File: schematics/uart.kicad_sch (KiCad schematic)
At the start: 7 parts, among them J10 myBus, J9 Pins, U8 74HC238, U9 W65C51N, X1 CXO_DIP8

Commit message: Fix errors in schematics
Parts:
- renumbered J9 to J7, J10 to J8

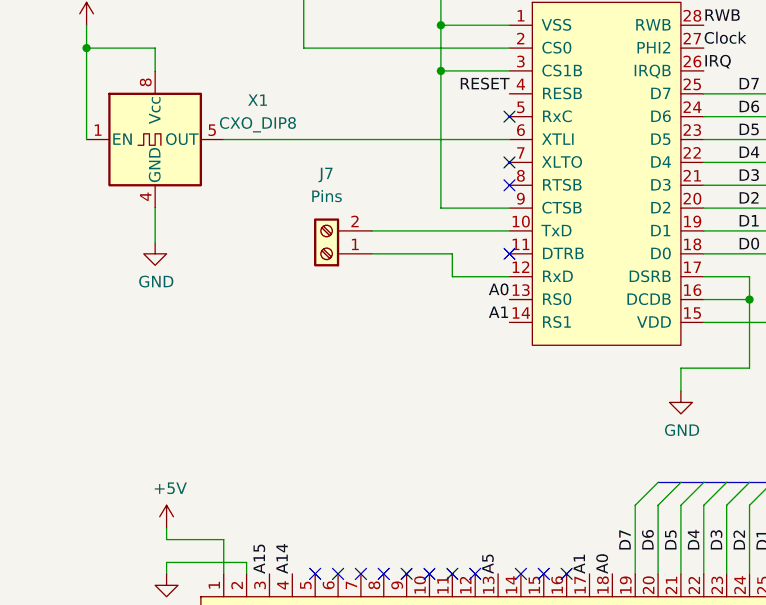
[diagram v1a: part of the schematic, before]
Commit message: Update shematics for UART & ESP
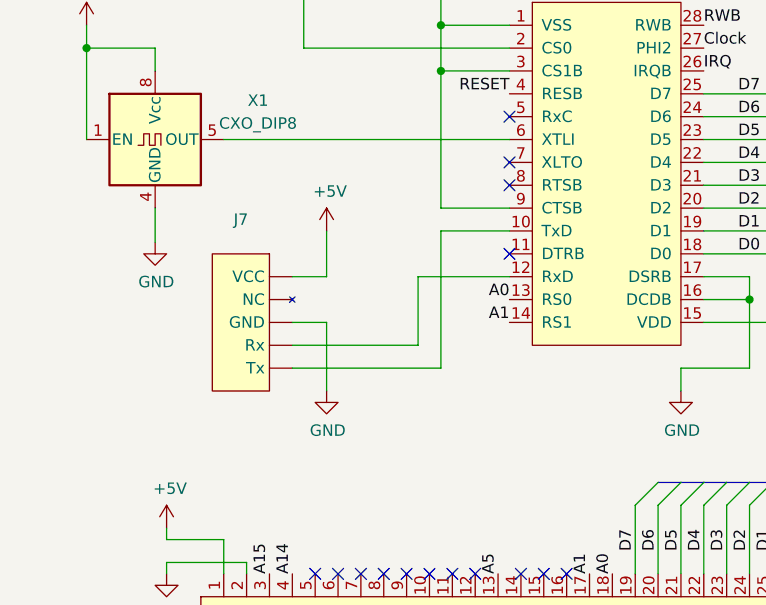
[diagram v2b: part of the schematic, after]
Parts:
- removed J7: Pins, symbol Connector:Screw_Terminal_01x02
- added J7: ~, symbol 6502:UART_connector
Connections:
- net +5V: now also J7. (VCC)
- net GND: now also J7. (VCC)
- net at U9.10 (TxD): now also J7. (VCC)
- net at U9.12 (RxD): now also J7. (VCC)
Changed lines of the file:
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@@
-		)
-	)
-	(wire
-		(pts
-			(xy 105.41 100.33) (xy 120.65 100.33)
-		)
-		(stroke
-			(width 0)
-			(type default)
 		)
 	)
@@
 		)
 	)
+	(wire
+		(pts
+			(xy 100.33 110.49) (xy 100.33 118.11)
+		)
+		(stroke
+			(width 0)
+			(type default)
+		)
+	)
 	(bus
 		(pts
@@
 	(wire
 		(pts
-			(xy 114.3 105.41) (xy 120.65 105.41)
+			(xy 113.03 100.33) (xy 120.65 100.33)
 		)
 		(stroke
@@
 	(wire
 		(pts
+			(xy 96.52 110.49) (xy 100.33 110.49)
+		)
+		(stroke
+			(width 0)
+			(type default)
+		)
+	)
+	(wire
+		(pts
 			(xy 88.9 90.17) (xy 120.65 90.17)
 		)
@@
 		)
 	)
+	(wire
+		(pts
+			(xy 110.49 105.41) (xy 110.49 113.03)
+		)
+		(stroke
+			(width 0)
+			(type default)
+		)
+	)
 	(bus
 		(pts
@@
 		)
 	)
+	(wire
+		(pts
+			(xy 96.52 105.41) (xy 100.33 105.41)
+		)
+		(stroke
+			(width 0)
+			(type default)
+		)
+	)
+	(wire
+		(pts
+			(xy 120.65 105.41) (xy 110.49 105.41)
+		)
+		(stroke
+			(width 0)
+			(type default)
+		)
+	)
 	(bus
 		(pts
@@
 	(wire
 		(pts
+			(xy 113.03 115.57) (xy 113.03 100.33)
+		)
+		(stroke
+			(width 0)
+			(type default)
+		)
+	)
+	(wire
+		(pts
 			(xy 68.58 67.31) (xy 68.58 68.58)
 		)
@@
 	(wire
 		(pts
-			(xy 105.41 102.87) (xy 114.3 102.87)
-		)
-		(stroke
-			(width 0)
-			(type default)
-		)
-	)
-	(wire
-		(pts
 			(xy 107.95 64.77) (xy 111.76 64.77)
 		)
@@
 	(wire
 		(pts
+			(xy 110.49 113.03) (xy 96.52 113.03)
+		)
+		(stroke
+			(width 0)
+			(type default)
+		)
+	)
+	(wire
+		(pts
 			(xy 119.38 64.77) (xy 123.19 64.77)
 		)
@@
 	(wire
 		(pts
+			(xy 100.33 105.41) (xy 100.33 100.33)
+		)
+		(stroke
+			(width 0)
+			(type default)
+		)
+	)
+	(wire
+		(pts
 			(xy 149.86 130.81) (xy 149.86 138.43)
 		)
@@
 	(wire
 		(pts
-			(xy 114.3 102.87) (xy 114.3 105.41)
+			(xy 96.52 115.57) (xy 113.03 115.57)
 		)
 		(stroke
@@
 	)
 	(symbol
-		(lib_id "Connector:Screw_Terminal_01x02")
-		(at 100.33 102.87 180)
+		(lib_id "6502:UART_connector")
+		(at 91.44 114.3 270)
 		(unit 1)
 		(exclude_from_sim no)
@@
 		(fields_autoplaced yes)
 		(property "Reference" "J7"
-			(at 100.33 93.98 0)
-			(effects
-				(font
-					(size 1.27 1.27)
-				)
-			)
-		)
-		(property "Value" "Pins"
-			(at 100.33 96.52 0)
+			(at 90.805 99.06 90)
+			(effects
+				(font
+					(size 1.27 1.27)
+				)
+			)
+		)
+		(property "Value" "~"
+			(at 90.805 101.6 90)
 			(effects
 				(font
@@
 		)
 		(property "Footprint" ""
-			(at 100.33 102.87 0)
-			(effects
-				(font
-					(size 1.27 1.27)
-				)
-				(hide yes)
-			)
-		)
-		(property "Datasheet" "~"
-			(at 100.33 102.87 0)
-			(effects
-				(font
-					(size 1.27 1.27)
-				)
-				(hide yes)
-			)
-		)
-		(property "Description" "Generic screw terminal, single row, 01x02, script generated (kicad-library-utils/schlib/autogen/connector/)"
-			(at 100.33 102.87 0)
+			(at 91.44 114.3 0)
+			(effects
+				(font
+					(size 1.27 1.27)
+				)
+				(hide yes)
+			)
+		)
+		(property "Datasheet" ""
+			(at 91.44 114.3 0)
+			(effects
+				(font
+					(size 1.27 1.27)
+				)
+				(hide yes)
+			)
+		)
+		(property "Description" ""
+			(at 91.44 114.3 0)
+			(effects
+				(font
+					(size 1.27 1.27)
+				)
+				(hide yes)
+			)
+		)
+		(pin ""
+		)
+		(pin ""
+		)
+		(pin ""
+		)
+		(pin ""
+		)
+		(pin ""
+		)
+		(instances
+			(project ""
+				(path "/03a78ca6-eaff-4f05-be7b-36cd15f8b56d/e1937880-b4d5-4732-8378-398cc9358f14"
+					(reference "J7")
+					(unit 1)
+				)
+			)
+		)
+	)
+	(symbol
+		(lib_id "power:GND")
+		(at 100.33 118.11 0)
+		(unit 1)
+		(exclude_from_sim no)
+		(in_bom yes)
+		(on_board yes)
+		(dnp no)
+		(property "Reference" "#PWR0101"
+			(at 100.33 124.46 0)
+			(effects
+				(font
+					(size 1.27 1.27)
+				)
+				(hide yes)
+			)
+		)
+		(property "Value" "GND"
+			(at 100.457 122.5042 0)
+			(effects
+				(font
+					(size 1.27 1.27)
+				)
+			)
+		)
+		(property "Footprint" ""
+			(at 100.33 118.11 0)
+			(effects
+				(font
+					(size 1.27 1.27)
+				)
+				(hide yes)
+			)
+		)
+		(property "Datasheet" ""
+			(at 100.33 118.11 0)
+			(effects
+				(font
+					(size 1.27 1.27)
+				)
+				(hide yes)
+			)
+		)
+		(property "Description" "Power symbol creates a global label with name \"GND\" , ground"
+			(at 100.33 118.11 0)
 			(effects
 				(font
@@
 		)
 		(pin "1"
-		)
-		(pin "2"
 		)
 		(instances
 			(project "markus"
 				(path "/03a78ca6-eaff-4f05-be7b-36cd15f8b56d/e1937880-b4d5-4732-8378-398cc9358f14"
-					(reference "J7")
+					(reference "#PWR0101")
 					(unit 1)
 				)
@@
 					(unit 1)
 				)
+			)
+		)
+	)
+	(symbol
+		(lib_id "power:+5V")
+		(at 100.33 100.33 0)
+		(unit 1)
+		(exclude_from_sim no)
+		(in_bom yes)
+		(on_board yes)
+		(dnp no)
+		(property "Reference" "#PWR0100"
+			(at 100.33 104.14 0)
+			(effects
+				(font
+					(size 1.27 1.27)
+				)
+				(hide yes)
+			)
+		)
+		(property "Value" "+5V"
+			(at 100.711 95.9358 0)
+			(effects
+				(font
+					(size 1.27 1.27)
+				)
+			)
+		)
+		(property "Footprint" ""
+			(at 100.33 100.33 0)
+			(effects
+				(font
+					(size 1.27 1.27)
+				)
+				(hide yes)
+			)
+		)
+		(property "Datasheet" ""
+			(at 100.33 100.33 0)
+			(effects
+				(font
+					(size 1.27 1.27)
+				)
+				(hide yes)
+			)
+		)
+		(property "Description" "Power symbol creates a global label with name \"+5V\""
+			(at 100.33 100.33 0)
+			(effects
+				(font
+					(size 1.27 1.27)
+				)
+				(hide yes)
+			)
+		)
+		(pin "1"
+		)
+		(instances
+			(project "markus"
+				(path "/03a78ca6-eaff-4f05-be7b-36cd15f8b56d/e1937880-b4d5-4732-8378-398cc9358f14"
+					(reference "#PWR0100")
+					(unit 1)
+				)

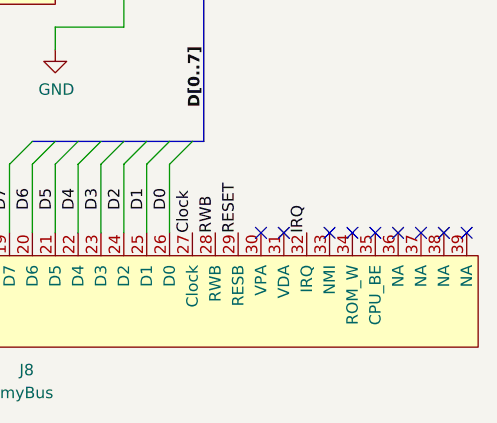
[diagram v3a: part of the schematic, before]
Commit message: Update ROM design
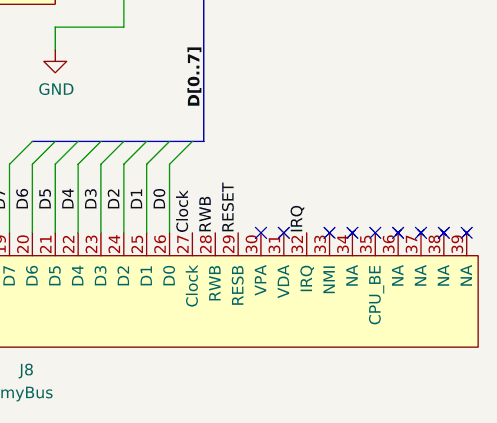
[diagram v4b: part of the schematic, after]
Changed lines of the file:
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@@
 	(label "D0"
 		(at 146.05 102.87 0)
-		(fields_autoplaced yes)
 		(effects
 			(font
@@
 	(label "A14"
 		(at 96.52 138.43 90)
-		(fields_autoplaced yes)
 		(effects
 			(font
@@
 	(label "RESET"
 		(at 120.65 85.09 180)
-		(fields_autoplaced yes)
 		(effects
 			(font
@@
 	(label "D1"
 		(at 146.05 100.33 0)
-		(fields_autoplaced yes)
 		(effects
 			(font
@@
 	(label "Clock"
 		(at 154.94 138.43 90)
-		(fields_autoplaced yes)
 		(effects
 			(font
@@
 	(label "D5"
 		(at 139.7 135.89 90)
-		(fields_autoplaced yes)
 		(effects
 			(font
@@
 	(label "D5"
 		(at 146.05 90.17 0)
-		(fields_autoplaced yes)
 		(effects
 			(font
@@
 	(label "D6"
 		(at 146.05 87.63 0)
-		(fields_autoplaced yes)
 		(effects
 			(font
@@
 	(label "D6"
 		(at 137.16 135.89 90)
-		(fields_autoplaced yes)
 		(effects
 			(font
@@
 	(label "D2"
 		(at 146.05 97.79 0)
-		(fields_autoplaced yes)
 		(effects
 			(font
@@
 	(label "Clock"
 		(at 142.24 80.01 0)
-		(fields_autoplaced yes)
 		(effects
 			(font
@@
 	(label "A5"
 		(at 73.66 54.61 180)
-		(fields_autoplaced yes)
 		(effects
 			(font
@@
 	(label "A1"
 		(at 120.65 110.49 180)
-		(fields_autoplaced yes)
 		(effects
 			(font
@@
 	(label "D7"
 		(at 134.62 135.89 90)
-		(fields_autoplaced yes)
 		(effects
 			(font
@@
 	(label "D4"
 		(at 146.05 92.71 0)
-		(fields_autoplaced yes)
 		(effects
 			(font
@@
 	(label "IRQ"
 		(at 142.24 82.55 0)
-		(fields_autoplaced yes)
 		(effects
 			(font
@@
 	(label "IRQ"
 		(at 167.64 138.43 90)
-		(fields_autoplaced yes)
 		(effects
 			(font
@@
 	(label "D0"
 		(at 152.4 135.89 90)
-		(fields_autoplaced yes)
 		(effects
 			(font
@@
 	(label "D1"
 		(at 149.86 135.89 90)
-		(fields_autoplaced yes)
 		(effects
 			(font
@@
 	(label "D3"
 		(at 146.05 95.25 0)
-		(fields_autoplaced yes)
 		(effects
 			(font
@@
 	(label "RWB"
 		(at 157.48 138.43 90)
-		(fields_autoplaced yes)
 		(effects
 			(font
@@
 	(label "D[0..7]"
 		(at 156.21 124.46 90)
-		(fields_autoplaced yes)
 		(effects
 			(font
@@
 	(label "RWB"
 		(at 142.24 77.47 0)
-		(fields_autoplaced yes)
 		(effects
 			(font
@@
 	(label "D7"
 		(at 146.05 85.09 0)
-		(fields_autoplaced yes)
 		(effects
 			(font
@@
 	(label "A0"
 		(at 132.08 138.43 90)
-		(fields_autoplaced yes)
 		(effects
 			(font
@@
 	(label "A5"
 		(at 119.38 138.43 90)
-		(fields_autoplaced yes)
 		(effects
 			(font
@@
 	(label "A15"
 		(at 73.66 49.53 180)
-		(fields_autoplaced yes)
 		(effects
 			(font
@@
 	(label "A1"
 		(at 129.54 138.43 90)
-		(fields_autoplaced yes)
 		(effects
 			(font
@@
 	(label "RESET"
 		(at 160.02 138.43 90)
-		(fields_autoplaced yes)
 		(effects
 			(font
@@
 	(label "D3"
 		(at 144.78 135.89 90)
-		(fields_autoplaced yes)
 		(effects
 			(font
@@
 	(label "D2"
 		(at 147.32 135.89 90)
-		(fields_autoplaced yes)
 		(effects
 			(font
@@
 	(label "A14"
 		(at 73.66 52.07 180)
-		(fields_autoplaced yes)
 		(effects
 			(font
@@
 	(label "A0"
 		(at 120.65 107.95 180)
-		(fields_autoplaced yes)
 		(effects
 			(font
@@
 	(label "A15"
 		(at 93.98 138.43 90)
-		(fields_autoplaced yes)
 		(effects
 			(font
@@
 	(label "D4"
 		(at 142.24 135.89 90)
-		(fields_autoplaced yes)
-		(effects
-			(font
+		(effects
+			(font

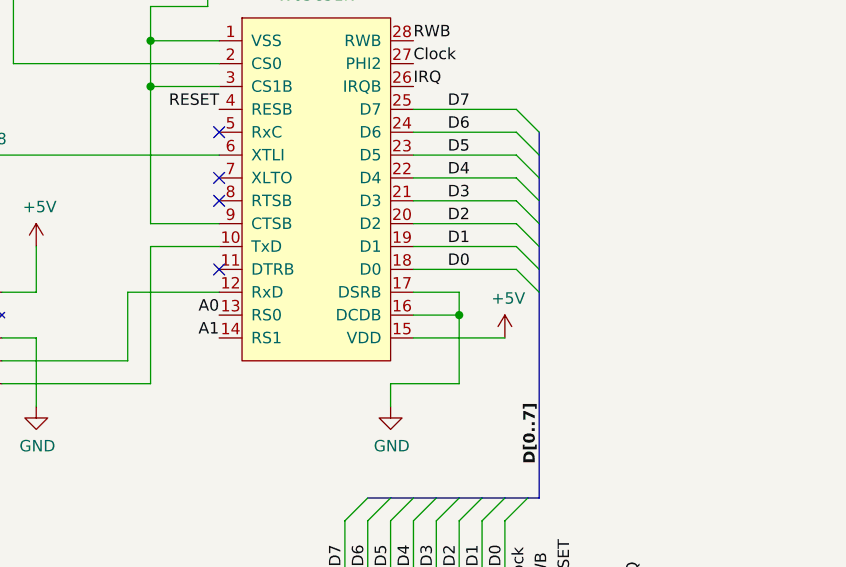
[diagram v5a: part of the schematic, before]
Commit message: Update UART schematics for flow control
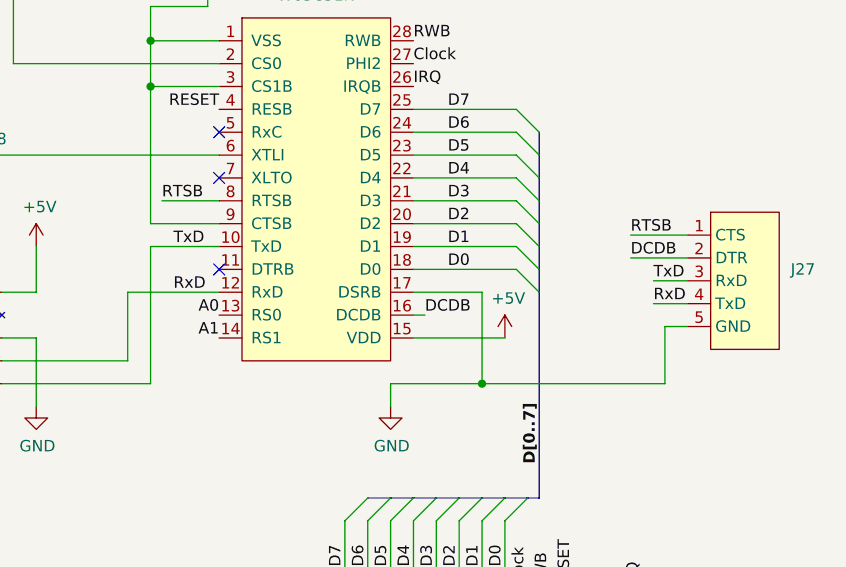
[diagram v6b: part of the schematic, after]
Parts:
- added J27: ~, symbol 6502:UART_connector_FC
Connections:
- net GND: now also J27.5 (GND); no longer U9.16 (DCDB)
- net TxD: now reaches J7. (Tx), U9.10 (TxD)
- net TxD: now also J27.3 (RxD)
- net RxD: now reaches J7. (Tx), U9.12 (RxD)
- net RxD: now also J27.4 (TxD)
- net RTSB: now reaches U9.8 (RTSB)
- net RTSB: now also J27.1 (CTS)
- new net DCDB: J27.2 (DTR), U9.16 (DCDB)
- no-connect marks 31 -> 30
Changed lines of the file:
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@@
-	)
-	(junction
-		(at 147.32 107.95)
-		(diameter 0)
-		(color 0 0 0 0)
 	)
 	(junction
@@
 	)
 	(junction
+		(at 149.86 115.57)
+		(diameter 0)
+		(color 0 0 0 0)
+	)
+	(junction
 		(at 97.79 64.77)
 		(diameter 0)
@@
 	)
 	(no_connect
-		(at 120.65 95.25)
-	)
-	(no_connect
 		(at 73.66 64.77)
 	)
@@
 		)
 	)
-	(wire
-		(pts
-			(xy 142.24 105.41) (xy 147.32 105.41)
-		)
-		(stroke
-			(width 0)
-			(type default)
-		)
-	)
 	(bus
 		(pts
@@
 	(wire
 		(pts
-			(xy 142.24 107.95) (xy 147.32 107.95)
-		)
-		(stroke
-			(width 0)
-			(type default)
-		)
-	)
-	(wire
-		(pts
 			(xy 142.24 102.87) (xy 153.67 102.87)
 		)
@@
 	(wire
 		(pts
-			(xy 147.32 105.41) (xy 147.32 107.95)
+			(xy 170.18 115.57) (xy 170.18 109.22)
 		)
 		(stroke
@@
 		)
 	)
+	(wire
+		(pts
+			(xy 168.91 104.14) (xy 172.72 104.14)
+		)
+		(stroke
+			(width 0)
+			(type default)
+		)
+	)
 	(bus
 		(pts
@@
 		)
 	)
+	(wire
+		(pts
+			(xy 170.18 109.22) (xy 172.72 109.22)
+		)
+		(stroke
+			(width 0)
+			(type default)
+		)
+	)
 	(bus
 		(pts
@@
 		)
 	)
+	(wire
+		(pts
+			(xy 149.86 105.41) (xy 149.86 115.57)
+		)
+		(stroke
+			(width 0)
+			(type default)
+		)
+	)
 	(bus
 		(pts
@@
 	(wire
 		(pts
-			(xy 147.32 115.57) (xy 139.7 115.57)
+			(xy 139.7 115.57) (xy 149.86 115.57)
 		)
 		(stroke
@@
 	(wire
 		(pts
+			(xy 142.24 105.41) (xy 149.86 105.41)
+		)
+		(stroke
+			(width 0)
+			(type default)
+		)
+	)
+	(wire
+		(pts
 			(xy 107.95 64.77) (xy 111.76 64.77)
 		)
@@
 	(wire
 		(pts
-			(xy 147.32 107.95) (xy 147.32 115.57)
-		)
-		(stroke
-			(width 0)
-			(type default)
-		)
-	)
-	(wire
-		(pts
 			(xy 142.24 92.71) (xy 153.67 92.71)
 		)
@@
 	(wire
 		(pts
+			(xy 142.24 107.95) (xy 143.51 107.95)
+		)
+		(stroke
+			(width 0)
+			(type default)
+		)
+	)
+	(wire
+		(pts
 			(xy 149.86 130.81) (xy 149.86 138.43)
 		)
@@
 	(wire
 		(pts
+			(xy 166.37 101.6) (xy 172.72 101.6)
+		)
+		(stroke
+			(width 0)
+			(type default)
+		)
+	)
+	(wire
+		(pts
 			(xy 142.24 87.63) (xy 153.67 87.63)
 		)
@@
 	(wire
 		(pts
+			(xy 114.3 95.25) (xy 120.65 95.25)
+		)
+		(stroke
+			(width 0)
+			(type default)
+		)
+	)
+	(wire
+		(pts
+			(xy 166.37 99.06) (xy 172.72 99.06)
+		)
+		(stroke
+			(width 0)
+			(type default)
+		)
+	)
+	(wire
+		(pts
 			(xy 73.66 62.23) (xy 66.04 62.23)
 		)
@@
 	(wire
 		(pts
+			(xy 149.86 115.57) (xy 170.18 115.57)
+		)
+		(stroke
+			(width 0)
+			(type default)
+		)
+	)
+	(wire
+		(pts
 			(xy 73.66 80.01) (xy 73.66 90.17)
 		)
@@
 		(pts
 			(xy 156.21 105.41) (xy 156.21 128.27)
+		)
+		(stroke
+			(width 0)
+			(type default)
+		)
+	)
+	(wire
+		(pts
+			(xy 168.91 106.68) (xy 172.72 106.68)
 		)
 		(stroke
@@
 		)
 	)
+	(label "DCDB"
+		(at 166.37 101.6 0)
+		(effects
+			(font
+				(size 1.27 1.27)
+			)
+			(justify left bottom)
+		)
+	)
 	(label "A14"
 		(at 96.52 138.43 90)
@@
 		)
 	)
+	(label "RTSB"
+		(at 166.37 99.06 0)
+		(effects
+			(font
+				(size 1.27 1.27)
+			)
+			(justify left bottom)
+		)
+	)
 	(label "D6"
 		(at 146.05 87.63 0)
@@
 		)
 	)
+	(label "TxD"
+		(at 115.57 100.33 0)
+		(effects
+			(font
+				(size 1.27 1.27)
+			)
+			(justify left bottom)
+		)
+	)
+	(label "RTSB"
+		(at 114.3 95.25 0)
+		(effects
+			(font
+				(size 1.27 1.27)
+			)
+			(justify left bottom)
+		)
+	)
 	(label "A1"
 		(at 120.65 110.49 180)
@@
 		)
 	)
+	(label "DCDB"
+		(at 143.51 107.95 0)
+		(effects
+			(font
+				(size 1.27 1.27)
+			)
+			(justify left bottom)
+		)
+	)
 	(label "D0"
 		(at 152.4 135.89 90)
@@
 		)
 	)
+	(label "TxD"
+		(at 168.91 104.14 0)
+		(effects
+			(font
+				(size 1.27 1.27)
+			)
+			(justify left bottom)
+		)
+	)
 	(label "RWB"
 		(at 142.24 77.47 0)
@@
 		)
 	)
+	(label "RxD"
+		(at 168.91 106.68 0)
+		(effects
+			(font
+				(size 1.27 1.27)
+			)
+			(justify left bottom)
+		)
+	)
 	(label "RESET"
 		(at 160.02 138.43 90)
+		(effects
+			(font
+				(size 1.27 1.27)
+			)
+			(justify left bottom)
+		)
+	)
+	(label "RxD"
+		(at 115.57 105.41 0)
 		(effects
 			(font
@@
 					(unit 1)
 				)
+			)
+		)
+	)
+	(symbol
+		(lib_id "6502:UART_connector_FC")
+		(at 177.8 95.25 0)
+		(unit 1)
+		(exclude_from_sim no)
+		(in_bom yes)
+		(on_board yes)
+		(dnp no)
+		(fields_autoplaced yes)
+		(property "Reference" "J27"
+			(at 184.15 102.8699 0)
+			(effects
+				(font
+					(size 1.27 1.27)
+				)
+				(justify left)
+			)
+		)
+		(property "Value" "~"
+			(at 184.15 105.4099 0)
+			(effects
+				(font
+					(size 1.27 1.27)
+				)
+				(justify left)
+			)
+		)
+		(property "Footprint" ""
+			(at 177.8 95.25 0)
+			(effects
+				(font
+					(size 1.27 1.27)
+				)
+				(hide yes)
+			)
+		)
+		(property "Datasheet" ""
+			(at 177.8 95.25 0)
+			(effects
+				(font
+					(size 1.27 1.27)
+				)
+				(hide yes)
+			)
+		)
+		(property "Description" ""
+			(at 177.8 95.25 0)
+			(effects
+				(font
+					(size 1.27 1.27)
+				)
+				(hide yes)
+			)
+		)
+		(pin "2"
+		)
+		(pin "5"
+		)
+		(pin "4"
+		)
+		(pin "3"
+		)
+		(pin "1"
+		)
+		(instances
+			(project ""
+				(path "/03a78ca6-eaff-4f05-be7b-36cd15f8b56d/e1937880-b4d5-4732-8378-398cc9358f14"
+					(reference "J27")
+					(unit 1)
+				)
